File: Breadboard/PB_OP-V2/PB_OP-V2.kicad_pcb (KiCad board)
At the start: 2 copper layers, 24 parts, among them J1 Conn_01x02_Pin, J2 Conn_01x02_Pin, J3 Conn_01x08_Pin, U1 NE5532

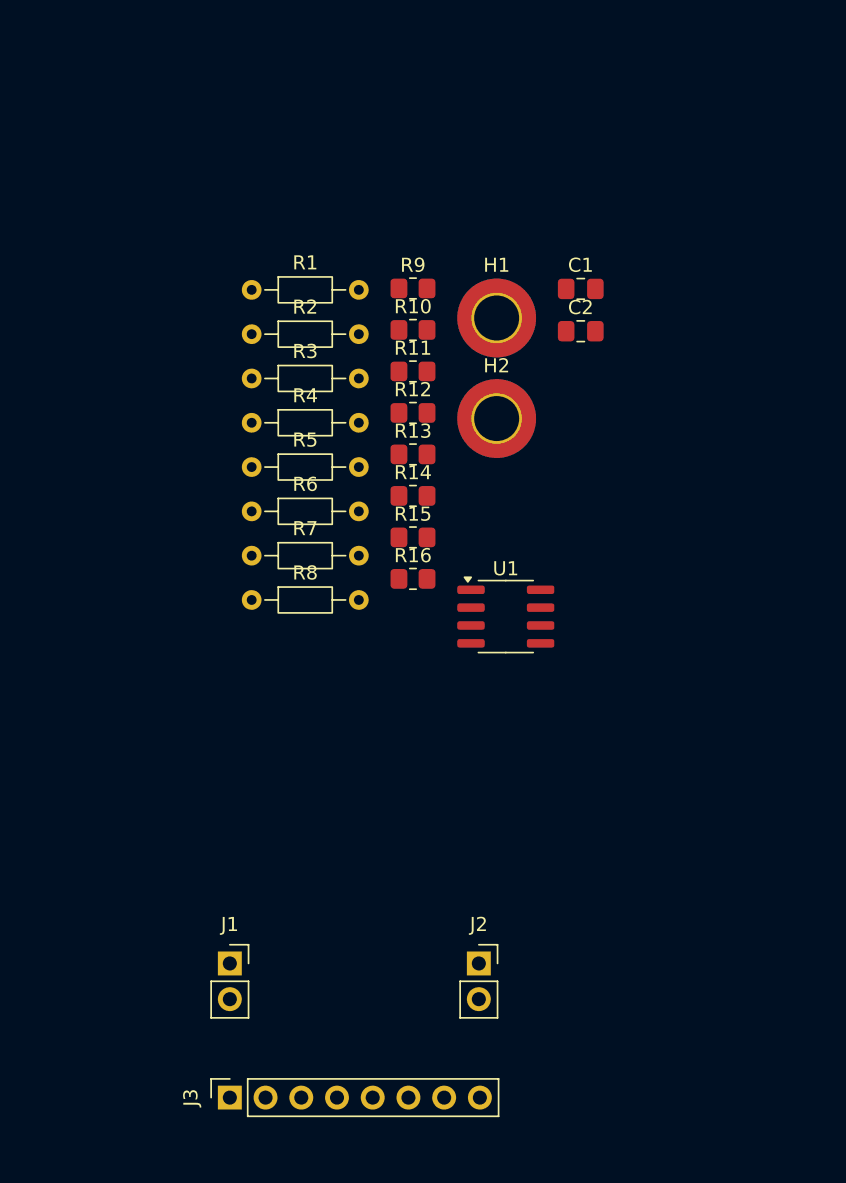
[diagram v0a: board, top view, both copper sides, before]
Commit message: Useless Adder auf V2.0 gebracht. Software finalisiert, Platine benötigt noch Arbeit
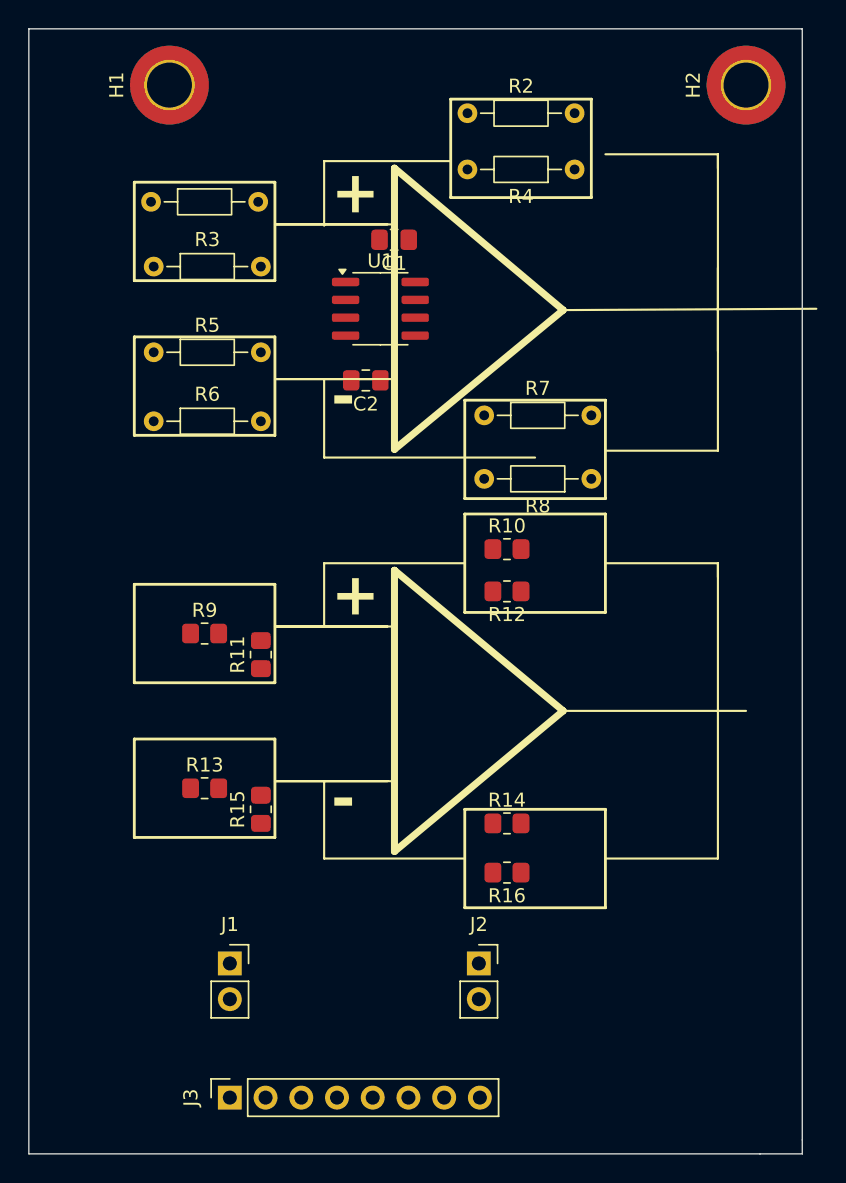
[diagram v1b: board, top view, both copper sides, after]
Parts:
- moved H2 29.6 mm to (230.0, 84.0), turned to 90 degrees
- moved R4 29.2 mm to (217.8, 90.0), turned to 180 degrees
- moved R9 28.7 mm to (191.5, 123.0)
- moved H1 28.6 mm to (189.0, 84.0), turned to 90 degrees
- moved R13 28.0 mm to (191.5, 134.0)
- moved R8 25.6 mm to (219.0, 112.0), turned to 180 degrees
- moved R14 24.2 mm to (213.0, 136.5)
- moved U1 23.6 mm to (204.0, 99.9)
- moved R11 22.9 mm to (195.5, 124.5), turned to 90 degrees
- moved R15 22.2 mm to (195.5, 135.5), turned to 90 degrees
- moved R2 22.0 mm to (210.2, 86.0)
- moved R16 21.9 mm to (213.0, 140.0), turned to 180 degrees
- moved R7 19.3 mm to (211.4, 107.5)
- moved R10 17.0 mm to (213.0, 117.0)
- moved C2 15.7 mm to (203.0, 105.0), turned to 180 degrees
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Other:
- board outline added: 55 x 80 mm
- board text added: "+ -"
